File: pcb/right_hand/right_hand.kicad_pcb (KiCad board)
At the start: 2 copper layers, 160 x 110 mm, 116 parts, among them J0 UJ20-C-H-G-SMT-P16-TR, U0 SW_Push

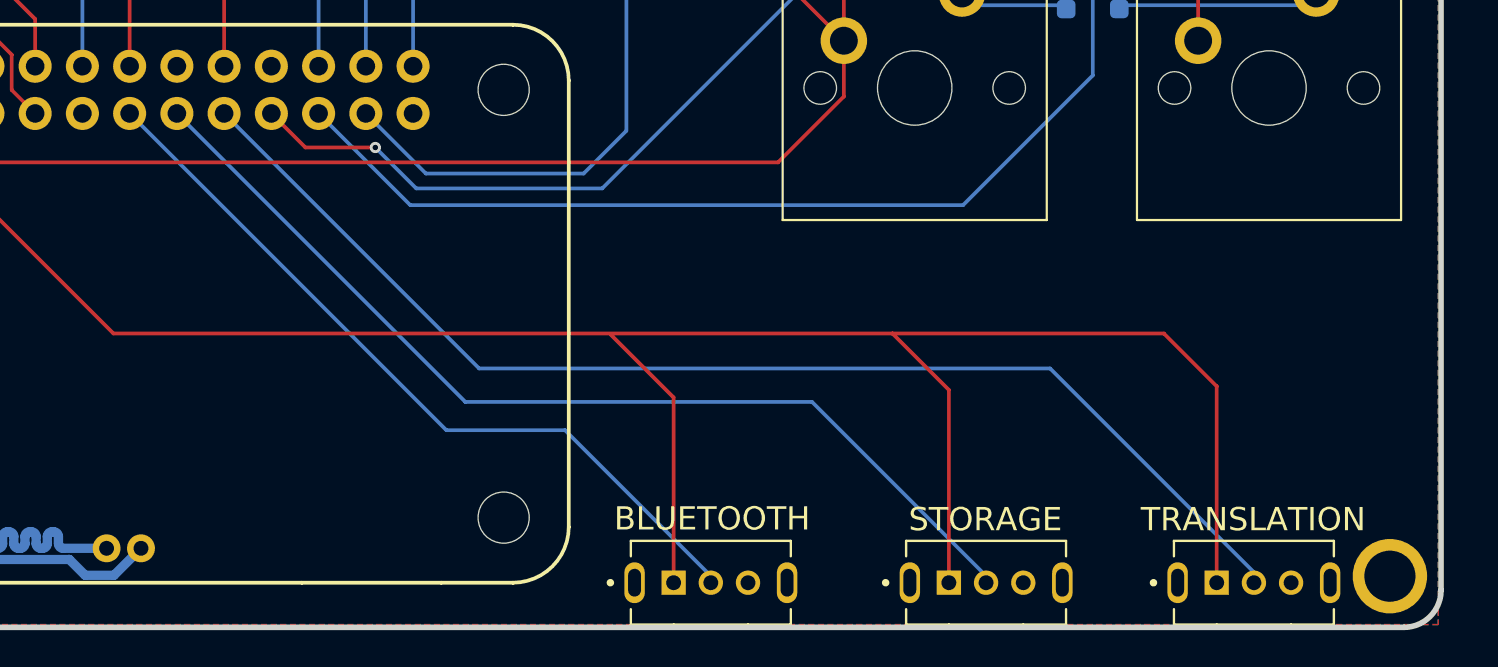
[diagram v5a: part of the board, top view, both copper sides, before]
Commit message: Move toggle switches closer together
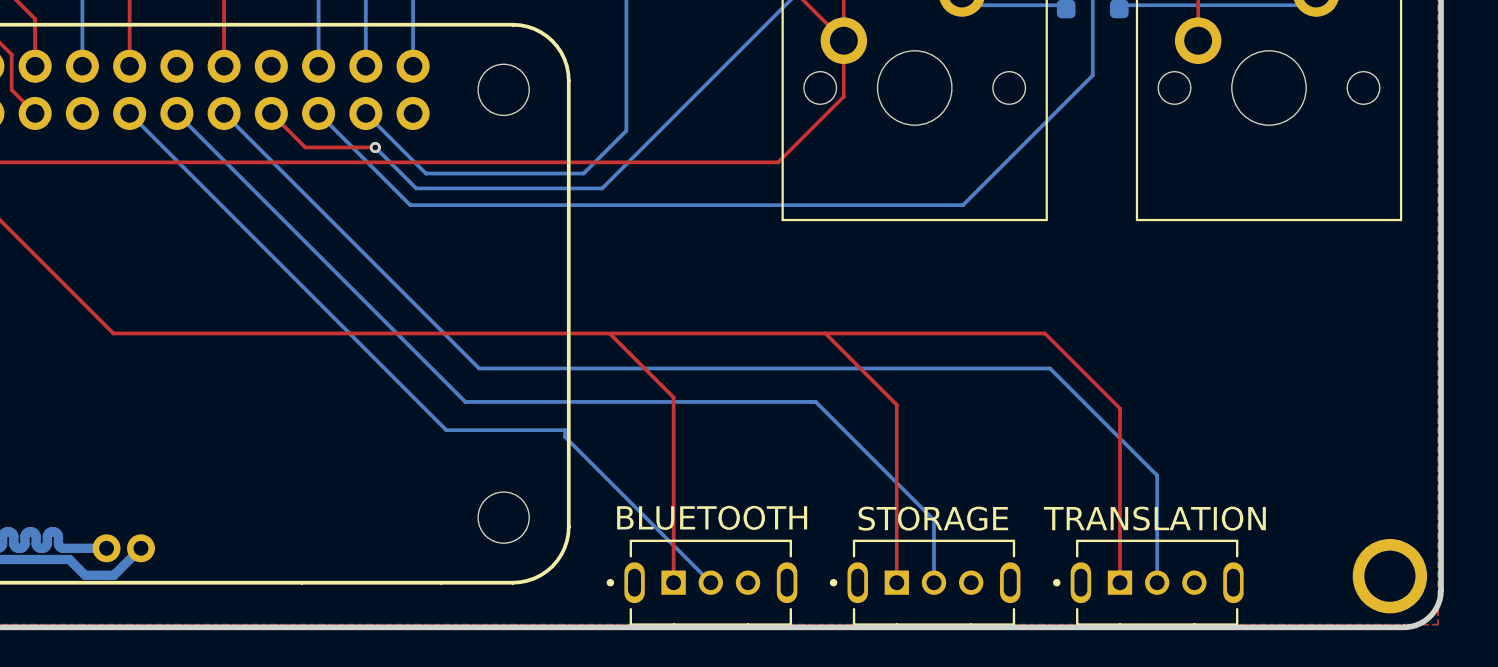
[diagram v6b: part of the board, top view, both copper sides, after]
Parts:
- moved TRANSLATION 5.20 mm to (214.0, 144.6)
- moved STORAGE 2.80 mm to (202.0, 144.6)
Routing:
- net Net-(A1-+3V3-Pad17): track 117.2 -> 111.6 mm
- net Net-(A1-GP6): track 66.1 -> 64.0 mm
- net Net-(A1-GP5): track 54.2 -> 53.2 mm
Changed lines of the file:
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@@
 	(footprint "snap_magic_footprints:SW_SLW-864587-2A-RA-N-D"
 		(layer "F.Cu")
-		(at 204.8375 144.6)
+		(at 202.0375 144.6)
 		(property "Reference" "STORAGE"
 			(at -0.0375 -3.4 0)
@@
 	(footprint "snap_magic_footprints:SW_SLW-864587-2A-RA-N-D"
 		(layer "F.Cu")
-		(at 219.2375 144.6)
+		(at 214.0375 144.6)
 		(property "Reference" "TRANSLATION"
 			(at -0.0375 -3.4 0)
@@
 	(segment
 		(start 157.92 131.2)
-		(end 199.8 131.2)
+		(end 196.2 131.2)
 		(width 0.2)
 		(layer "F.Cu")
@@
 	)
 	(segment
-		(start 199.8 131.2)
-		(end 214.4 131.2)
+		(start 196.2 131.2)
+		(end 208 131.2)
 		(width 0.2)
 		(layer "F.Cu")
@@
 	)
 	(segment
-		(start 202.8375 134.2375)
-		(end 202.8375 144.6)
+		(start 200.0375 135.0375)
+		(end 196.2 131.2)
 		(width 0.2)
 		(layer "F.Cu")
@@
 	)
 	(segment
-		(start 188.0375 144.6)
-		(end 188.0375 134.6375)
+		(start 200.0375 144.6)
+		(end 200.0375 135.0375)
 		(width 0.2)
 		(layer "F.Cu")
@@
 	)
 	(segment
-		(start 214.4 131.2)
-		(end 217.2375 134.0375)
+		(start 188.0375 144.6)
+		(end 188.0375 134.6375)
 		(width 0.2)
 		(layer "F.Cu")
@@
 	)
 	(segment
-		(start 199.8 131.2)
-		(end 202.8375 134.2375)
+		(start 212.0375 135.2375)
+		(end 212.0375 144.6)
 		(width 0.2)
 		(layer "F.Cu")
@@
 	)
 	(segment
-		(start 217.2375 134.0375)
-		(end 217.2375 144.6)
+		(start 208 131.2)
+		(end 212.0375 135.2375)
 		(width 0.2)
 		(layer "F.Cu")
@@
 	)
 	(segment
-		(start 190.0375 144.2375)
-		(end 182.2 136.4)
+		(start 175.82 136.4)
+		(end 158.79 119.37)
 		(width 0.2)
 		(layer "B.Cu")
@@
 	)
 	(segment
-		(start 175.82 136.4)
-		(end 158.79 119.37)
+		(start 190.0375 144.6)
+		(end 190.0375 144.2375)
 		(width 0.2)
 		(layer "B.Cu")
@@
 	)
 	(segment
-		(start 190.0375 144.6)
-		(end 190.0375 144.2375)
+		(start 182.2 136.4)
+		(end 182.2 136.7625)
+		(width 0.2)
+		(layer "B.Cu")
+		(net 79)
+	)
+	(segment
+		(start 182.2 136.7625)
+		(end 190.0375 144.6)
 		(width 0.2)
 		(layer "B.Cu")
@@
 	)
 	(segment
-		(start 163.87 119.37)
-		(end 177.58125 133.08125)
+		(start 214.0375 144.6)
+		(end 214.0375 138.8375)
 		(width 0.2)
 		(layer "B.Cu")
@@
 	)
 	(segment
-		(start 177.58125 133.08125)
+		(start 214.0375 138.8375)
 		(end 208.28125 133.08125)
 		(width 0.2)
@@
 	)
 	(segment
-		(start 219.2375 144.0375)
-		(end 219.2375 144.6)
+		(start 208.28125 133.08125)
+		(end 177.58125 133.08125)
 		(width 0.2)
 		(layer "B.Cu")
@@
 	)
 	(segment
-		(start 208.28125 133.08125)
-		(end 219.2375 144.0375)
+		(start 177.58125 133.08125)
+		(end 163.87 119.37)
 		(width 0.2)
 		(layer "B.Cu")
@@
 	(segment
 		(start 176.84125 134.88125)
-		(end 195.48125 134.88125)
+		(end 195.4 134.88125)
 		(width 0.2)
 		(layer "B.Cu")
@@
 	)
 	(segment
-		(start 195.48125 134.88125)
-		(end 204.8375 144.2375)
+		(start 195.4 134.88125)
+		(end 195.68125 134.88125)
+		(width 0.2)
+		(layer "B.Cu")
+		(net 81)
+	)
+	(segment
+		(start 202.0375 141.2375)
+		(end 202.0375 144.6)
 		(width 0.2)
 		(layer "B.Cu")
@@
 	)
 	(segment
-		(start 204.8375 144.2375)
-		(end 204.8375 144.6)
+		(start 195.68125 134.88125)
+		(end 202.0375 141.2375)
+		(width 0.2)
+		(layer "B.Cu")
+		(net 81)
+	)
+	(segment
+		(start 195.4 134.88125)
+		(end 195.48125 134.88125)
 		(width 0.2)
 		(layer "B.Cu")
